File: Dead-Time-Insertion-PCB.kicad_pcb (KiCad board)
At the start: 2 copper layers, 24.1 x 22.9 mm, 16 parts, among them J1 Conn_01x08_Male, Q1 MMBT3904, Q2 MMBT3904, Q3 MMBT3904, Q4 MMBT3904, Q5 MMBT3904, Q6 MMBT3904, Q7 MMBT3904, U1 74HC86

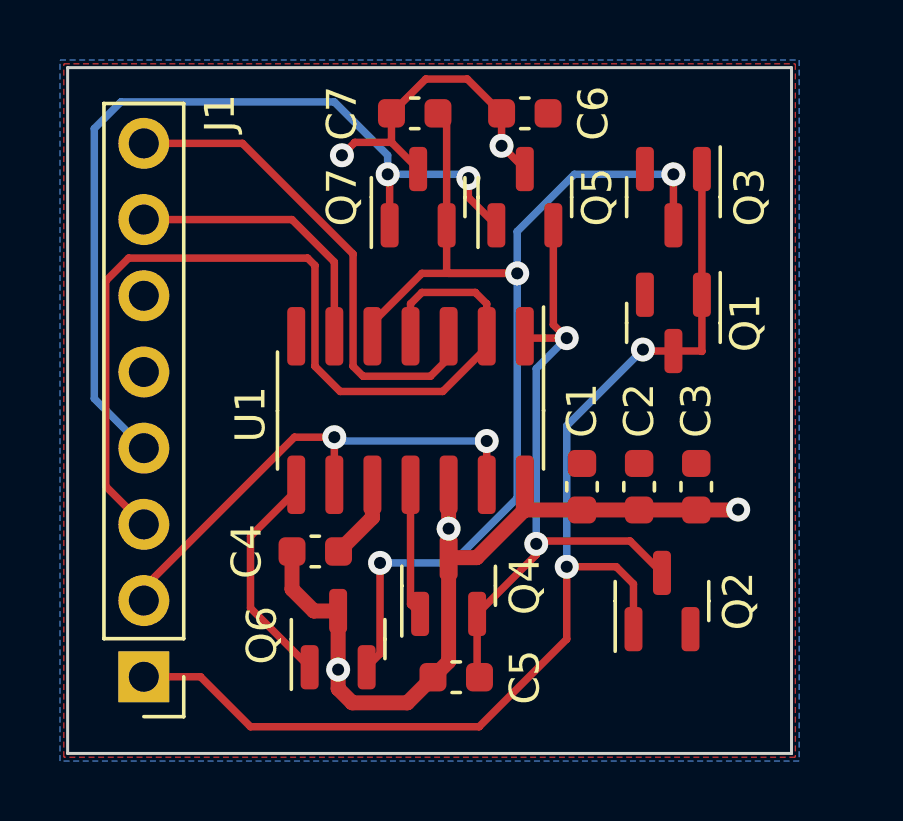
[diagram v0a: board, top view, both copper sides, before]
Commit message: added voltage regulator so I don't blow this board up with 12V
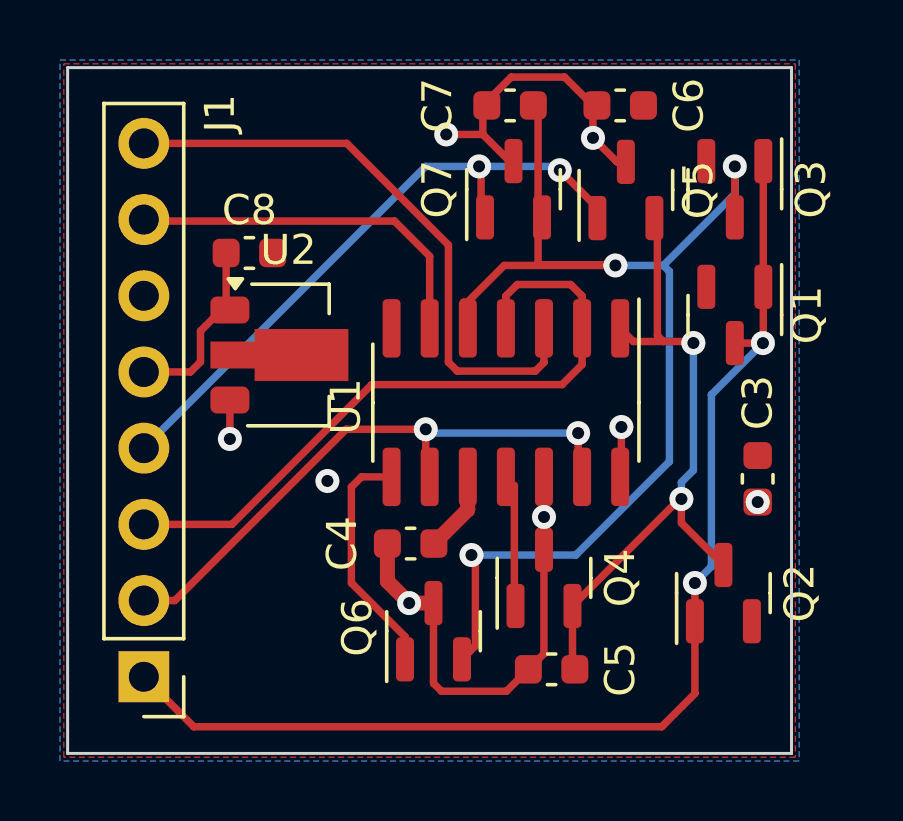
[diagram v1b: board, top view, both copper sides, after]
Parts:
- removed C1: 1n, Capacitor_SMD:C_0603_1608Metric
- removed C2: 10n, Capacitor_SMD:C_0603_1608Metric
- added C8: 100n, Capacitor_SMD:C_0603_1608Metric, F.Cu at (118.2, 72.6)
- added U2: L7805, Package_TO_SOT_SMD:SOT-89-3, F.Cu at (119.5, 76.0)
- moved Q5 3.38 mm to (130.8, 70.5)
- moved Q4 3.19 mm to (128.0, 83.4)
- moved Q6 3.19 mm to (124.3, 85.2)
- moved Q7 3.19 mm to (127.0, 70.5)
- moved C4 3.19 mm to (123.6, 82.3)
- moved C5 3.19 mm to (128.3, 86.5)
- moved C6 3.19 mm to (130.6, 67.7)
- moved C7 3.19 mm to (126.9, 67.7)
- moved U1 3.19 mm to (126.8, 77.6)
- moved C3 2.06 mm to (135.1, 80.1)
- moved Q1 2.06 mm to (134.4, 74.7)
- moved Q3 2.06 mm to (134.4, 70.5)
- moved Q2 2.06 mm to (134.0, 83.9)
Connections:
- C3 pad 1: VCC -> +5V
- C4 pad 1: VCC -> +5V
- C5 pad 1: VCC -> +5V
- C6 pad 1: VCC -> +5V
- C7 pad 1: VCC -> +5V
- Q4 pad 3: VCC -> +5V
- Q5 pad 3: VCC -> +5V
- Q6 pad 3: VCC -> +5V
- Q7 pad 3: VCC -> +5V
- U1 pad 12: VCC -> +5V
- U1 pad 14: VCC -> +5V
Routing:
- net VCC: track 38.9 -> 6.28 mm, vias 5 -> 0
- net +5V: track 0.00 -> 29.5 mm, vias 0 -> 7
- net /INVERT_OUTPUT: track 31.5 -> 23.0 mm
- net /~{ENABLE}: track 29.3 -> 21.7 mm
- net /OUT_H: track 16.5 -> 20.1 mm
- net /INPUT: track 17.0 -> 20.4 mm
- net /OUT_L: track 9.41 -> 12.6 mm
- net Net-(Q6-B): track 7.53 -> 8.16 mm
- net Net-(Q3-C): track 39.4 -> 40.1 mm
- net GND: vias 0 -> 1
- added copper zone on B.Cu, net +5V
- removed copper zone on B.Cu, net VCC

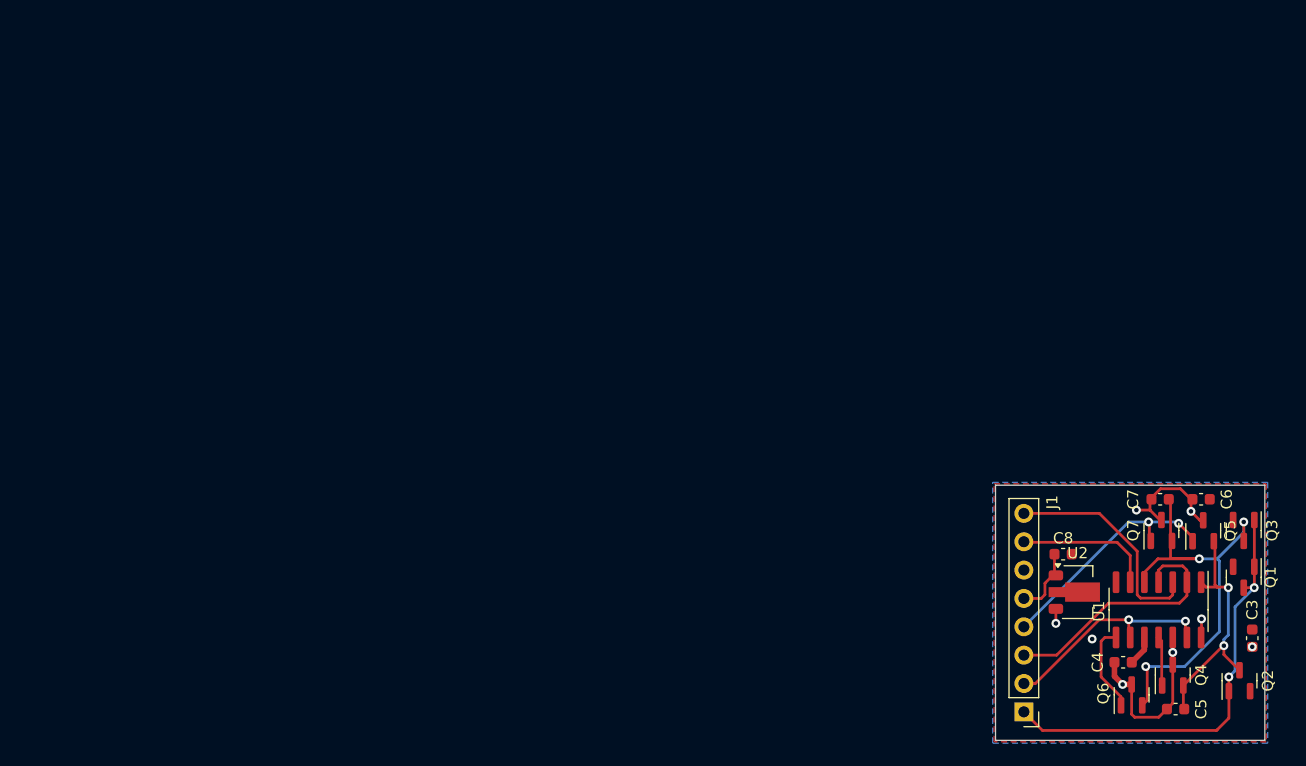
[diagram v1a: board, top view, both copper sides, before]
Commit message: addressed parasitic oscillations by adding pulldown/pullup resistors, overhauling the PCB layout to reduce the footprint of sensitive nodes, took great care to avoid cross coupling of input and output signals, added a stupid amount of vias since they are free, and improved the current sinks by replacing the package with a SOT363 transistor array to have better matching between diode-connected BJT and current sink BJT
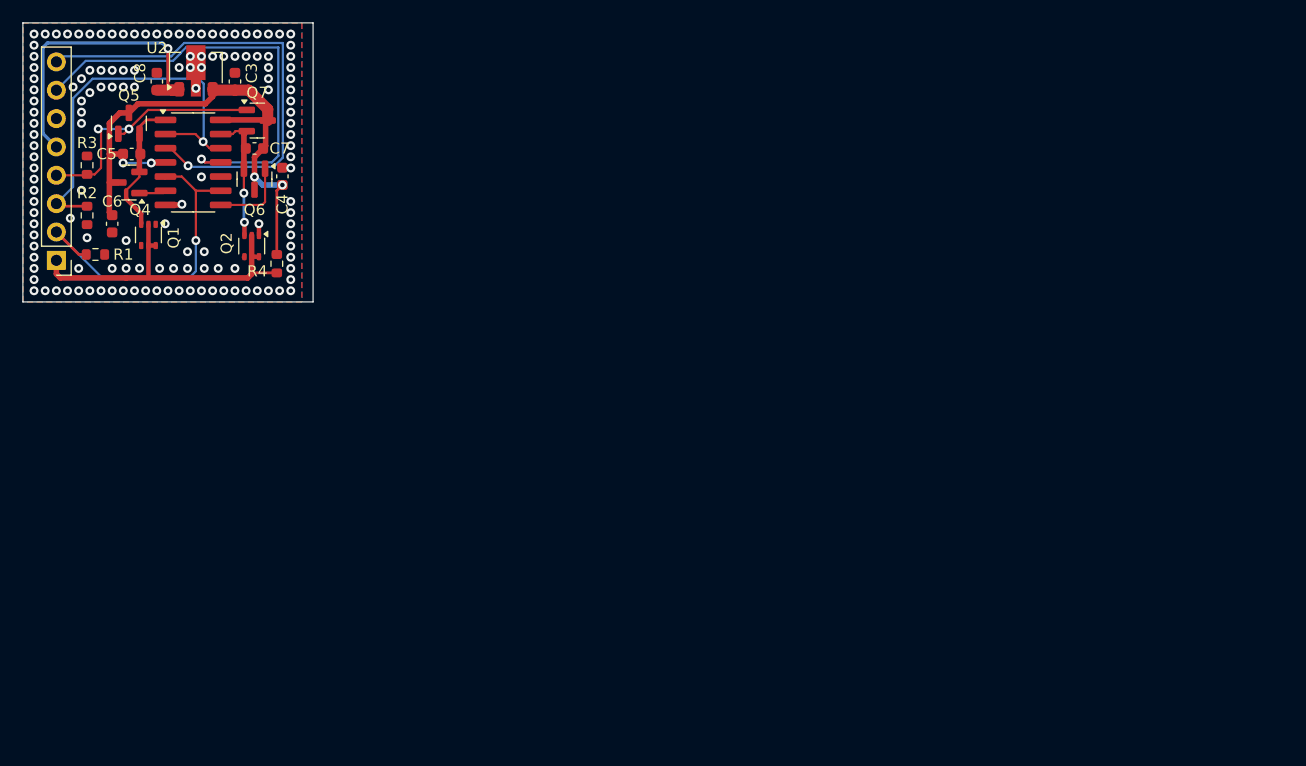
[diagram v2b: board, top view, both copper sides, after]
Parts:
- removed Q3: MMBT3904, Package_TO_SOT_SMD:SOT-23
- added R1: 1k, Resistor_SMD:R_0603_1608Metric, F.Cu at (31.5, 45.8)
- added R2: 1k, Resistor_SMD:R_0603_1608Metric, F.Cu at (30.8, 42.2)
- added R3: 1k, Resistor_SMD:R_0603_1608Metric, F.Cu at (30.8, 37.8)
- added R4: R, Resistor_SMD:R_0603_1608Metric, F.Cu at (47.8, 46.6)
- Q1, Q2: value MMBT3904 -> FFB3904; footprint Package_TO_SOT_SMD:SOT-23 -> Package_TO_SOT_SMD:SOT-363_SC-70-6
- moved C5 105.9 mm to (34.8, 36.8)
- moved C3 103.9 mm to (44.0, 30.2)
- moved Q4 103.4 mm to (34.5, 39.3), turned to 180 degrees
- moved Q5 102.9 mm to (34.5, 34.0)
- moved Q1 102.8 mm to (36.2, 44.0)
- moved C6 100.6 mm to (33.0, 43.0), turned to -90 degrees
- moved Q2 96.7 mm to (45.5, 45.0), turned to -90 degrees
- moved J1 95.7 mm to (28.0, 46.3)
- moved U1 95.3 mm to (40.2, 37.5), turned to 0 degrees
- moved U2 91.9 mm to (40.5, 29.0), turned to 90 degrees
- moved C8 91.6 mm to (37.0, 30.2), turned to 90 degrees
- moved Q6 91.2 mm to (45.8, 39.0), turned to -90 degrees
- moved Q7 88.9 mm to (46.0, 33.8), turned to 0 degrees
- moved C7 87.0 mm to (45.8, 36.2), turned to 180 degrees
- moved C4 87.0 mm to (48.2, 38.8), turned to 90 degrees
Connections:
- C5 pad 2: Net-(Q2-C) -> /H
- C7 pad 2: Net-(Q3-C) -> /L
- Q1 pad 1: /DEAD_TIME_CTRL -> GND
- Q1 pad 2: GND -> /DEAD_TIME_CTRL
- Q1 pad 3: /DEAD_TIME_CTRL -> /H
- Q2 pad 1: /DEAD_TIME_CTRL -> GND
- Q2 pad 2: GND -> /DEAD_TIME_CTRL
- Q2 pad 3: Net-(Q2-C) -> /L
- Q4 pad 2: Net-(Q2-C) -> /H
- Q5 pad 2: Net-(Q2-C) -> /H
- Q6 pad 2: Net-(Q3-C) -> /L
- Q7 pad 2: Net-(Q3-C) -> /L
- U1 pad 1: Net-(Q2-C) -> /H
- U1 pad 11: Net-(Q4-B) -> /OUT_L
- U1 pad 12: +5V -> /INVERT_OUTPUT
- U1 pad 13: /INPUT -> /L
- U1 pad 4: /INVERT_OUTPUT -> +5V
- U1 pad 5: Net-(Q3-C) -> /INPUT
- U1 pad 6: /OUT_L -> Net-(Q4-B)
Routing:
- net Net-(Q3-C): track 40.1 -> 0.00 mm, vias 3 -> 0
- net /OUT_L: track 12.6 -> 40.6 mm, vias 0 -> 1
- net /OUT_H: track 20.1 -> 42.9 mm, vias 0 -> 1
- net Net-(Q2-C): track 22.5 -> 0.00 mm, vias 2 -> 0
- net +5V: track 29.5 -> 51.9 mm, vias 7 -> 4
- net VCC: track 6.28 -> 27.2 mm, vias 0 -> 1
- net /INVERT_OUTPUT: track 23.0 -> 36.2 mm, vias 0 -> 1
- net /H: track 0.00 -> 12.4 mm
- net /L: track 0.00 -> 12.1 mm, vias 0 -> 2
- net /INPUT: track 20.4 -> 30.7 mm, vias 2 -> 1
- net /DEAD_TIME_CTRL: track 39.0 -> 30.6 mm, vias 2 -> 0
- net Net-(Q4-B): track 4.44 -> 2.42 mm
- net /~{ENABLE}: track 21.7 -> 23.3 mm
- net GND: track 3.39 -> 2.62 mm, vias 1 -> 140
- added copper zone on B.Cu, net GND
- removed copper zone on B.Cu, net +5V
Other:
- board size 24.1 x 22.9 mm -> 26 x 25 mm
- board text added: "OUT_H OUT_L GND VCC ~{EN} INVERT INPUT DEADTIME_CTRL"
- board text removed: "OUT_H OUT_L GND VCC ~EN INVERT INPUT DEADTIME_CTRL"
